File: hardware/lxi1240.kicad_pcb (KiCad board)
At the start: 2 copper layers, 105.4 x 62.2 mm, 1 part, among them J230 1240COMM

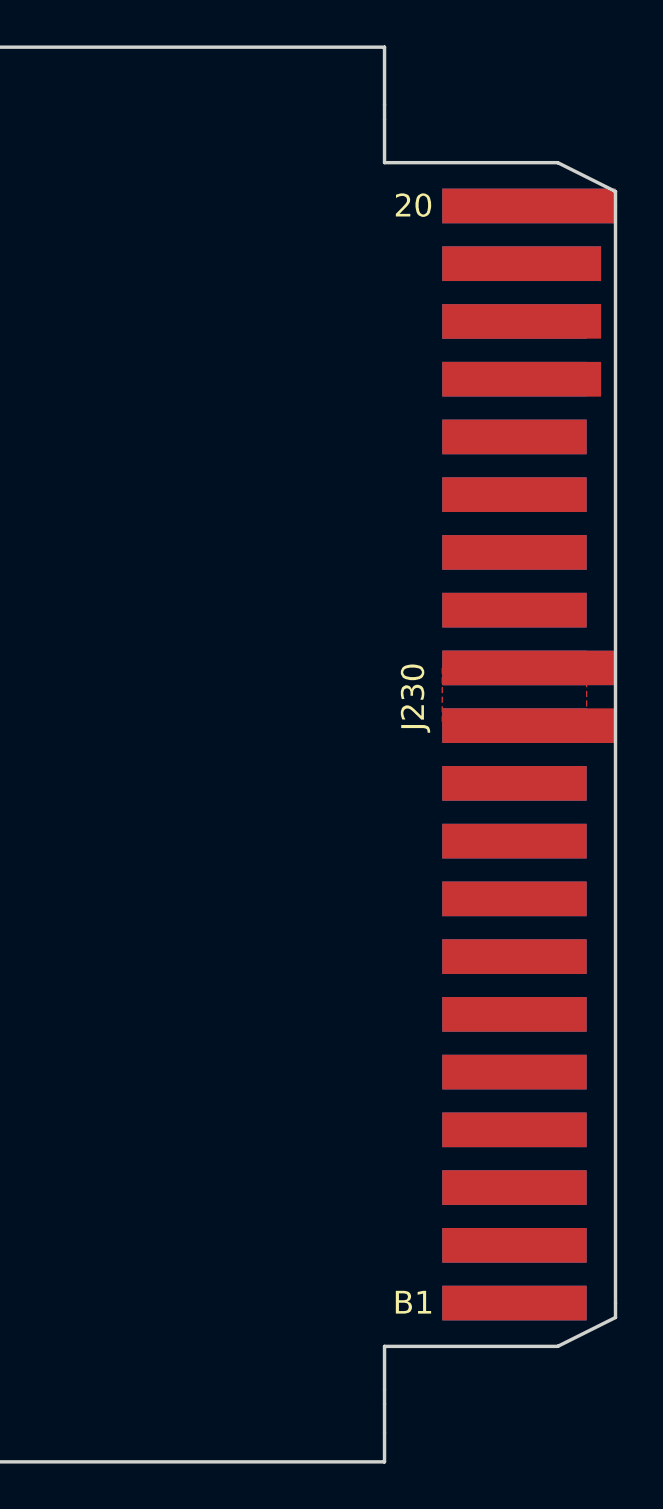
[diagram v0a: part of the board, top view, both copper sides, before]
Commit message: Add a breakout header for the board edge connector.
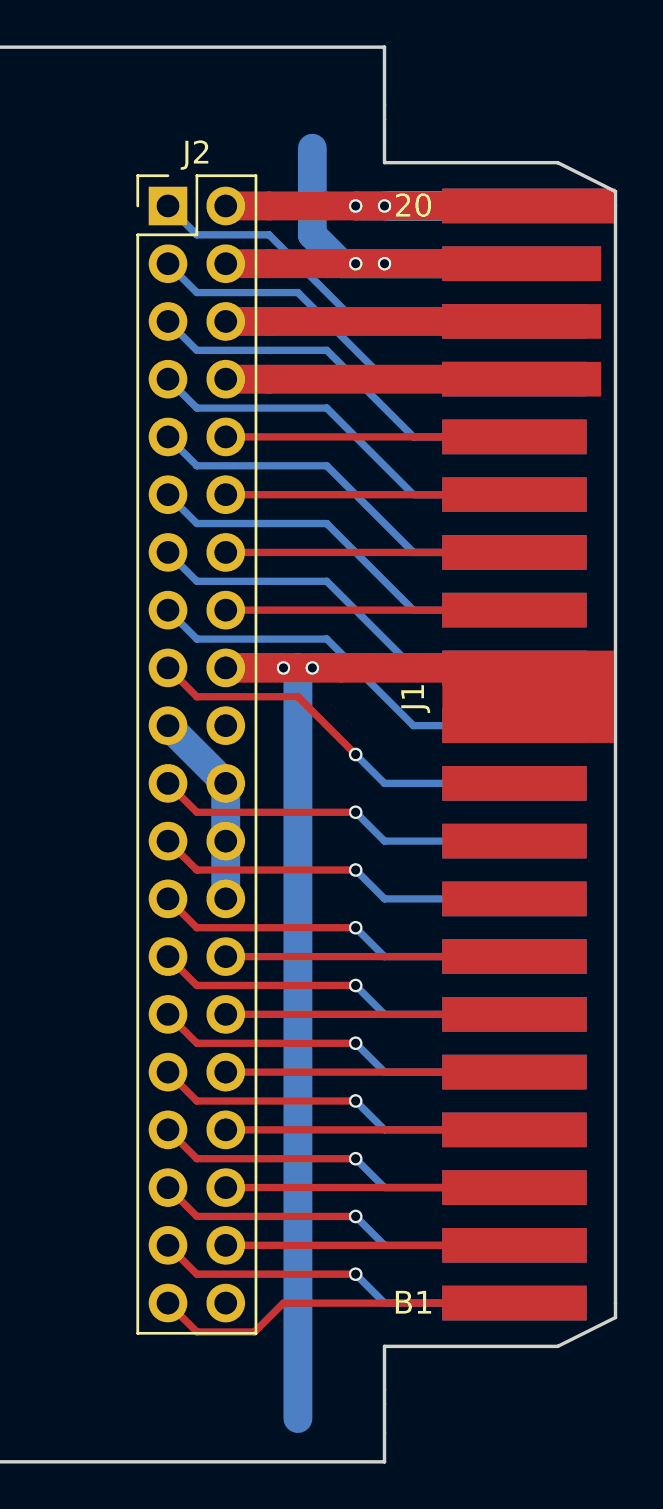
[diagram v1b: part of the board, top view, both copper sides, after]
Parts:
- added J2: 1240COMM_EXT, Pin_Headers:Pin_Header_Straight_2x20_Pitch2.54mm, F.Cu at (205.1, 64.8)
- renumbered J230 to J1
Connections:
- J1 pad A1: Net-(J230-PadA1) -> /~H-WR
- J1 pad A10: /D2 -> /H-D2
- J1 pad A11: /D0 -> /H-D0
- J1 pad A13: Net-(J230-PadA13) -> /~H-RS
- J1 pad A14: Net-(J230-PadA14) -> /H-INT
- J1 pad A15: Net-(J230-PadA15) -> /~H-RD
- J1 pad A16: /A0 -> /H-A0
- J1 pad A17: /A2 -> /H-A2
- J1 pad A18: /A4 -> /H-A4
- J1 pad A2: Net-(J230-PadA2) -> /H-RST
- J1 pad A3: /A5 -> /H-A5
- J1 pad A4: /D1 -> /H-D1
- J1 pad A5: /D3 -> /H-D3
- J1 pad A6: /D5 -> /H-D5
- J1 pad A7: /D7 -> /H-D7
- J1 pad A8: /D6 -> /H-D6
- J1 pad A9: /D4 -> /H-D4
- J1 pad B1: /A1 -> /H-A1
- J1 pad B13: /A12 -> /H-A12
- J1 pad B14: /A10 -> /H-A10
- J1 pad B15: /A8 -> /H-A8
- J1 pad B16: /A6 -> /H-A6
- J1 pad B17: Net-(J230-PadB17) -> +12VA
- J1 pad B18: Net-(J230-PadB18) -> -12VA
- J1 pad B2: /A3 -> /H-A3
- J1 pad B3: Net-(J230-PadB3) -> /~H-CS
- J1 pad B4: /A7 -> /H-A7
- J1 pad B5: /A9 -> /H-A9
- J1 pad B6: /A11 -> /H-A11
- J1 pad B7: /A13 -> /H-A13
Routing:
- net Earth_Protective: track 0.00 -> 52.1 mm, vias 0 -> 2
- net GND: track 0.00 -> 24.5 mm, vias 0 -> 2
- net +5V: track 0.00 -> 22.1 mm, vias 0 -> 2
- net /H-A0: track 0.00 -> 14.2 mm
- net Net-(J1-PadA12): track 0.00 -> 14.2 mm
- net /~H-RS: track 0.00 -> 14.2 mm
- net /~H-RD: track 0.00 -> 14.2 mm
- net /H-INT: track 0.00 -> 14.2 mm
- net /H-D2: track 0.00 -> 14.2 mm, vias 0 -> 1
- net /H-D0: track 0.00 -> 14.2 mm
- net /H-A4: track 0.00 -> 14.2 mm
- net /H-A2: track 0.00 -> 14.2 mm
- net /~H-WR: track 0.00 -> 13.1 mm, vias 0 -> 1
- net /H-D7: track 0.00 -> 13.1 mm, vias 0 -> 1
- net /H-D6: track 0.00 -> 13.1 mm, vias 0 -> 1
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- removed copper zone on F.Cu, net Earth_Protective
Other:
- net class Default: trace_width 0.25 -> 0.32258
- net class Power added: clearance 0.2, trace_width 1.27, via_dia 0.6, via_drill 0.4
- net class SGND removed
- rule trace_min: 0.2 -> 0.1524
- rule via_min_drill: 0.3 -> 0.254
- rule via_min_size: 0.4 -> 0.254
- board text added: "+12"
- board text added: "+5"
- board text added: "-12"
- board text added: "A0"
- board text added: "A1"
- board text added: "A10"
- board text added: "A11"
- board text added: "A12"
- board text added: "A13"
- board text added: "A2"
- board text added: "A3"
- board text added: "A4"
- board text added: "A5"
- board text added: "A6"
- board text added: "A7"
- board text added: "A8"
- board text added: "A9"
- board text added: "D0"
- board text added: "D1"
- board text added: "D2"
- board text added: "D3"
- board text added: "D4"
- board text added: "D5"
- board text added: "D6"
- board text added: "D7"
- board text added: "GND"
- board text added: "INT"
- board text added: "OSC"
- board text added: "PE"
- board text added: "RST"
- board text added: "USE 80-CONDUCTOR ATA RIBBON"
- board text added: "~CS"
- board text added: "~RD"
- board text added: "~RS"
- board text added: "~WR"

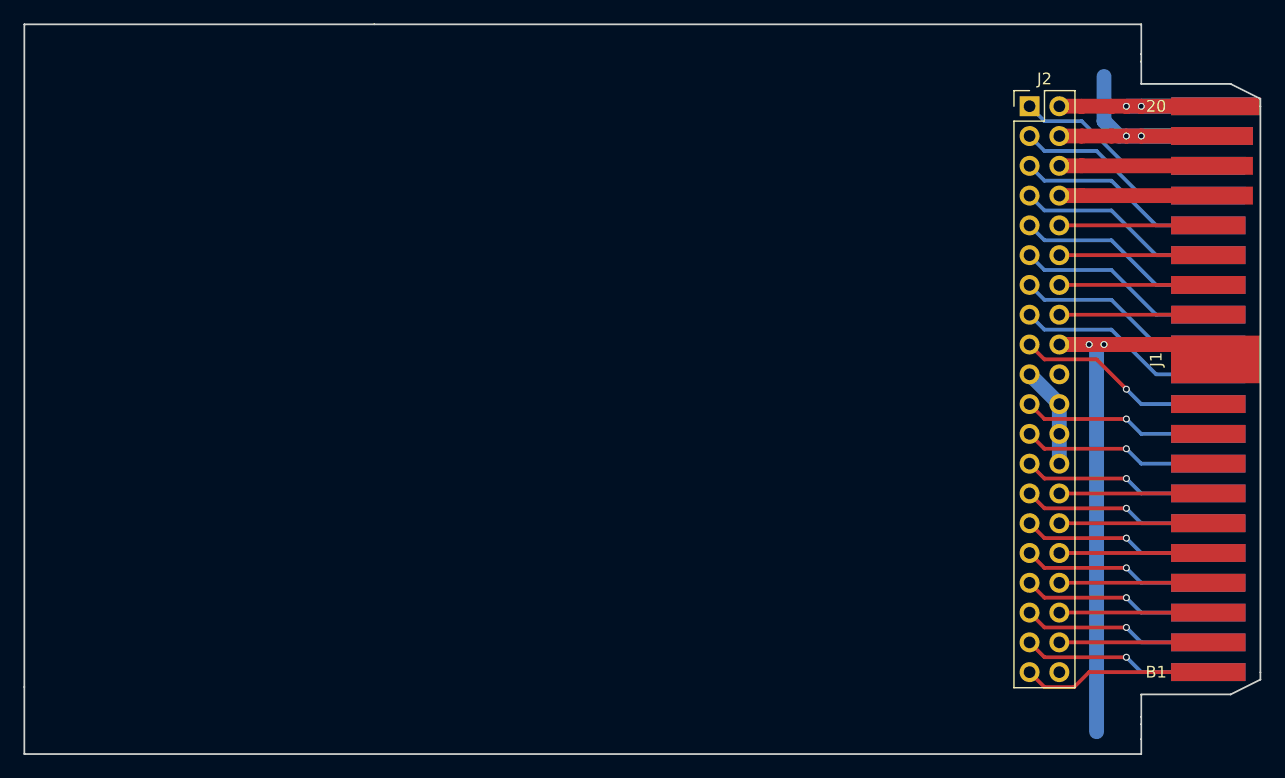
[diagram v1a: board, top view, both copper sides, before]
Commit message: Add mounting holes with protective ground.
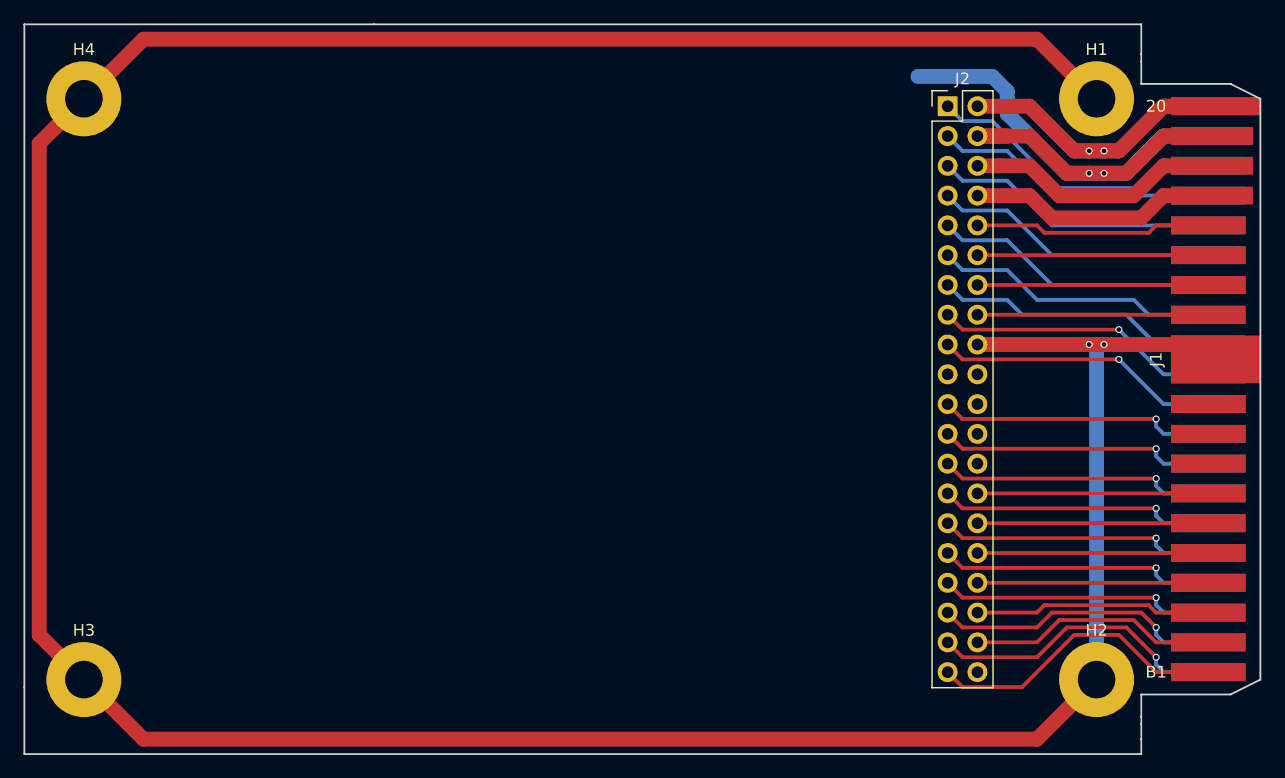
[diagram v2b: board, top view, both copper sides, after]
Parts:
- added H1: Mount, Mounting_Holes:MountingHole_3.2mm_M3_Pad, F.Cu at (210.8, 64.1)
- added H2: Mount, Mounting_Holes:MountingHole_3.2mm_M3_Pad, F.Cu at (210.8, 113.7)
- added H3: Mount, Mounting_Holes:MountingHole_3.2mm_M3_Pad, F.Cu at (124.5, 113.7)
- added H4: Mount, Mounting_Holes:MountingHole_3.2mm_M3_Pad, F.Cu at (124.5, 64.1)
- moved J2 6.98 mm to (198.1, 64.8)
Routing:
- net Earth_Protective: track 52.1 -> 280.2 mm
- net +5V: track 22.1 -> 52.7 mm
- net GND: track 24.5 -> 38.5 mm
- net /H-A1: track 13.1 -> 22.7 mm
- net /~H-WR: track 13.1 -> 22.6 mm
- net -12VA: track 9.52 -> 18.6 mm
- net /H-A3: track 9.52 -> 18.1 mm
- net +12VA: track 9.52 -> 18.1 mm
- net /H-A4: track 14.2 -> 22.7 mm
- net /H-RST: track 13.1 -> 21.5 mm
- net /~H-CS: track 9.52 -> 17.0 mm
- net /H-A6: track 9.52 -> 17.0 mm
- net /H-D7: track 13.1 -> 20.5 mm
- net /H-D4: track 13.1 -> 20.5 mm
- net /H-D3: track 13.1 -> 20.5 mm
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
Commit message: Add ground pours.
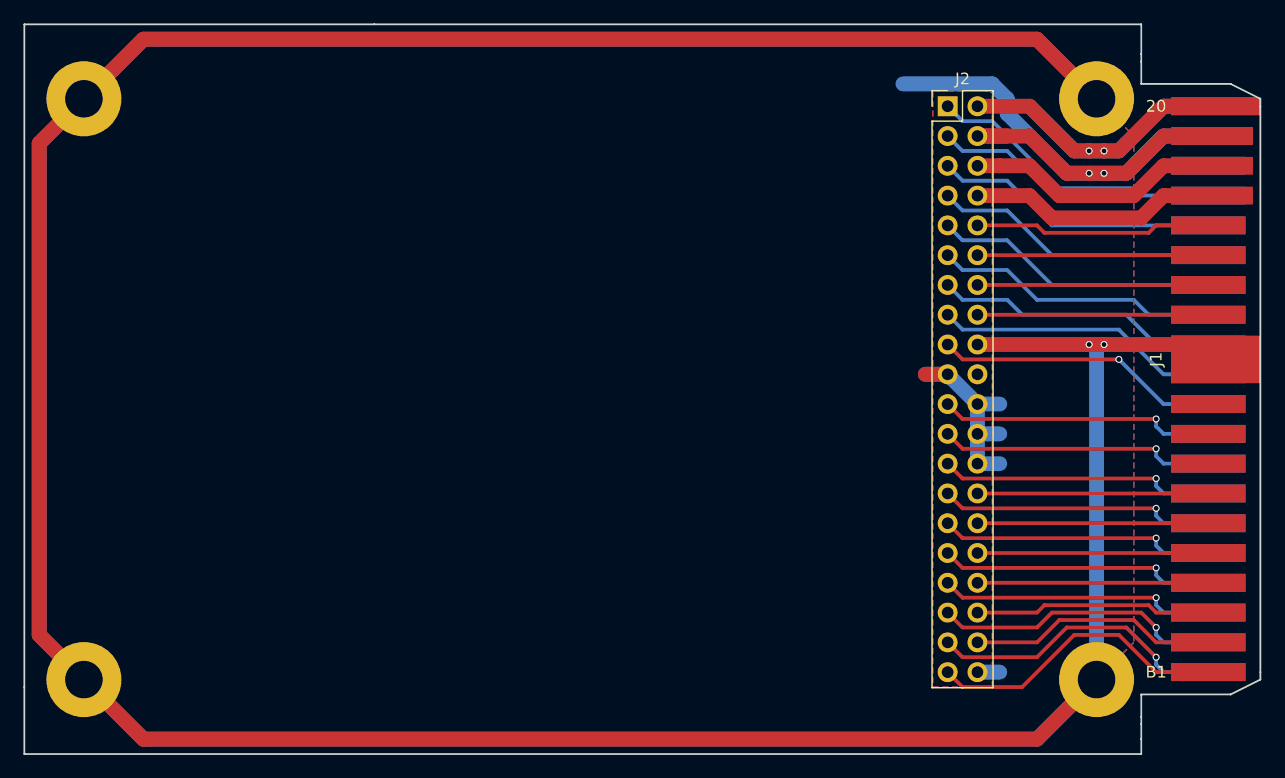
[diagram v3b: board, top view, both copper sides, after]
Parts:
- renumbered H2 to H1, H3 to H2, H4 to H3, H1 to H4
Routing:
- net Earth_Protective: track 280.2 -> 514.0 mm
- net GND: track 38.5 -> 58.6 mm
- net +5V: track 52.7 -> 53.3 mm
- net /H-D0: vias 1 -> 0
- added copper zone on B.Cu, net GND
- added copper zone on F.Cu, net GND

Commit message: Remove pad for key pin in ATA header.
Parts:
- J2: footprint Pin_Headers:Pin_Header_Straight_2x20_Pitch2.54mm -> 1240comm:ATA_HEADER
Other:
- board text added: "USE 80-CONDUCTOR ATA RIBBON DO NOT USE SLAVE CONNECTOR"
- board text removed: "USE 80-CONDUCTOR ATA RIBBON"
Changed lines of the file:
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@@
     (zones 0)
     (modules 6)
-    (nets 39)
+    (nets 38)
   )
   (page A4)
@@
     (46 B.CrtYd user)
     (47 F.CrtYd user)
-    (48 B.Fab user hide)
-    (49 F.Fab user hide)
+    (48 B.Fab user)
+    (49 F.Fab user)
   )
   (setup
@@
     (pad_to_mask_clearance 0.2)
     (aux_axis_origin 0 0)
-    (visible_elements FFFEFFFF)
+    (visible_elements FFFEEF7F)
     (pcbplotparams
       (layerselection 0x00030_80000001)
@@
   (net 36 /H-A2)
   (net 37 /H-A4)
-  (net 38 "Net-(J2-Pad20)")
   (net_class Default "This is the default net class."
     (clearance 0.2)
@@
     (add_net "Net-(J1-PadB8)")
     (add_net "Net-(J1-PadB9)")
-    (add_net "Net-(J2-Pad20)")
   )
   (net_class Power ""
@@
       (net 1 GND))
   )
-  (module Pin_Headers:Pin_Header_Straight_2x20_Pitch2.54mm (layer F.Cu)
+  (module Mounting_Holes:MountingHole_3.2mm_M3_Pad (layer F.Cu)
+    (at 210.82 64.135)
+    (descr "Mounting Hole 3.2mm, M3")
+    (tags "mounting hole 3.2mm m3")
+    (attr virtual)
+    (fp_text reference H4 (at 0 -4.445) (layer F.SilkS) hide
+      (effects (font (size 1 1) (thickness 0.15)))
+    )
+    (fp_text value Mount (at 0 4.2) (layer F.Fab)
+      (effects (font (size 1 1) (thickness 0.15)))
+    )
+    (fp_text user %R (at 0.3 0) (layer F.Fab)
+      (effects (font (size 1 1) (thickness 0.15)))
+    )
+    (fp_circle (center 0 0) (end 3.2 0) (layer Cmts.User) (width 0.15))
+    (fp_circle (center 0 0) (end 3.45 0) (layer F.CrtYd) (width 0.05))
+    (pad 1 thru_hole circle (at 0 0) (size 6.4 6.4) (drill 3.2) (layers *.Cu *.Mask)
+      (net 3 Earth_Protective))
+  )
+  (module Mounting_Holes:MountingHole_3.2mm_M3_Pad (layer F.Cu)
+    (at 210.82 113.665)
+    (descr "Mounting Hole 3.2mm, M3")
+    (tags "mounting hole 3.2mm m3")
+    (attr virtual)
+    (fp_text reference H1 (at 0 4.445) (layer F.SilkS) hide
+      (effects (font (size 1 1) (thickness 0.15)))
+    )
+    (fp_text value Mount (at 0 4.2) (layer F.Fab)
+      (effects (font (size 1 1) (thickness 0.15)))
+    )
+    (fp_text user %R (at 0.3 0) (layer F.Fab)
+      (effects (font (size 1 1) (thickness 0.15)))
+    )
+    (fp_circle (center 0 0) (end 3.2 0) (layer Cmts.User) (width 0.15))
+    (fp_circle (center 0 0) (end 3.45 0) (layer F.CrtYd) (width 0.05))
+    (pad 1 thru_hole circle (at 0 0) (size 6.4 6.4) (drill 3.2) (layers *.Cu *.Mask)
+      (net 3 Earth_Protective))
+  )
+  (module Mounting_Holes:MountingHole_3.2mm_M3_Pad (layer F.Cu)
+    (at 124.46 113.665)
+    (descr "Mounting Hole 3.2mm, M3")
+    (tags "mounting hole 3.2mm m3")
+    (attr virtual)
+    (fp_text reference H2 (at 0 4.445) (layer F.SilkS) hide
+      (effects (font (size 1 1) (thickness 0.15)))
+    )
+    (fp_text value Mount (at 0 4.2) (layer F.Fab)
+      (effects (font (size 1 1) (thickness 0.15)))
+    )
+    (fp_text user %R (at 0.3 0) (layer F.Fab)
+      (effects (font (size 1 1) (thickness 0.15)))
+    )
+    (fp_circle (center 0 0) (end 3.2 0) (layer Cmts.User) (width 0.15))
+    (fp_circle (center 0 0) (end 3.45 0) (layer F.CrtYd) (width 0.05))
+    (pad 1 thru_hole circle (at 0 0) (size 6.4 6.4) (drill 3.2) (layers *.Cu *.Mask)
+      (net 3 Earth_Protective))
+  )
+  (module Mounting_Holes:MountingHole_3.2mm_M3_Pad (layer F.Cu)
+    (at 124.46 64.135)
+    (descr "Mounting Hole 3.2mm, M3")
+    (tags "mounting hole 3.2mm m3")
+    (attr virtual)
+    (fp_text reference H3 (at 0 -4.445) (layer F.SilkS) hide
+      (effects (font (size 1 1) (thickness 0.15)))
+    )
+    (fp_text value Mount (at 0 4.2) (layer F.Fab)
+      (effects (font (size 1 1) (thickness 0.15)))
+    )
+    (fp_text user %R (at 0.3 0) (layer F.Fab)
+      (effects (font (size 1 1) (thickness 0.15)))
+    )
+    (fp_circle (center 0 0) (end 3.2 0) (layer Cmts.User) (width 0.15))
+    (fp_circle (center 0 0) (end 3.45 0) (layer F.CrtYd) (width 0.05))
+    (pad 1 thru_hole circle (at 0 0) (size 6.4 6.4) (drill 3.2) (layers *.Cu *.Mask)
+      (net 3 Earth_Protective))
+  )
+  (module 1240comm:ATA_HEADER (layer F.Cu)
     (at 198.12 64.77)
     (descr "Through hole straight pin header, 2x20, 2.54mm pitch, double rows")
@@
     (pad 19 thru_hole oval (at 0 22.86) (size 1.7 1.7) (drill 1) (layers *.Cu *.Mask)
       (net 1 GND))
-    (pad 20 thru_hole oval (at 2.54 22.86) (size 1.7 1.7) (drill 1) (layers *.Cu *.Mask)
-      (net 38 "Net-(J2-Pad20)"))
     (pad 21 thru_hole oval (at 0 25.4) (size 1.7 1.7) (drill 1) (layers *.Cu *.Mask)
       (net 28 /H-D4))
@@
     )
   )
-  (module Mounting_Holes:MountingHole_3.2mm_M3_Pad (layer F.Cu)
-    (at 210.82 64.135)
-    (descr "Mounting Hole 3.2mm, M3")
-    (tags "mounting hole 3.2mm m3")
-    (attr virtual)
-    (fp_text reference H4 (at 0 -4.445) (layer F.SilkS) hide
-      (effects (font (size 1 1) (thickness 0.15)))
-    )
-    (fp_text value Mount (at 0 4.2) (layer F.Fab)
-      (effects (font (size 1 1) (thickness 0.15)))
-    )
-    (fp_text user %R (at 0.3 0) (layer F.Fab)
-      (effects (font (size 1 1) (thickness 0.15)))
-    )
-    (fp_circle (center 0 0) (end 3.2 0) (layer Cmts.User) (width 0.15))
-    (fp_circle (center 0 0) (end 3.45 0) (layer F.CrtYd) (width 0.05))
-    (pad 1 thru_hole circle (at 0 0) (size 6.4 6.4) (drill 3.2) (layers *.Cu *.Mask)
-      (net 3 Earth_Protective))
-  )
-  (module Mounting_Holes:MountingHole_3.2mm_M3_Pad (layer F.Cu)
-    (at 210.82 113.665)
-    (descr "Mounting Hole 3.2mm, M3")
-    (tags "mounting hole 3.2mm m3")
-    (attr virtual)
-    (fp_text reference H1 (at 0 4.445) (layer F.SilkS) hide
-      (effects (font (size 1 1) (thickness 0.15)))
-    )
-    (fp_text value Mount (at 0 4.2) (layer F.Fab)
-      (effects (font (size 1 1) (thickness 0.15)))
-    )
-    (fp_text user %R (at 0.3 0) (layer F.Fab)
-      (effects (font (size 1 1) (thickness 0.15)))
-    )
-    (fp_circle (center 0 0) (end 3.2 0) (layer Cmts.User) (width 0.15))
-    (fp_circle (center 0 0) (end 3.45 0) (layer F.CrtYd) (width 0.05))
-    (pad 1 thru_hole circle (at 0 0) (size 6.4 6.4) (drill 3.2) (layers *.Cu *.Mask)
-      (net 3 Earth_Protective))
-  )
-  (module Mounting_Holes:MountingHole_3.2mm_M3_Pad (layer F.Cu)
-    (at 124.46 113.665)
-    (descr "Mounting Hole 3.2mm, M3")
-    (tags "mounting hole 3.2mm m3")
-    (attr virtual)
-    (fp_text reference H2 (at 0 4.445) (layer F.SilkS) hide
-      (effects (font (size 1 1) (thickness 0.15)))
-    )
-    (fp_text value Mount (at 0 4.2) (layer F.Fab)
-      (effects (font (size 1 1) (thickness 0.15)))
-    )
-    (fp_text user %R (at 0.3 0) (layer F.Fab)
-      (effects (font (size 1 1) (thickness 0.15)))
-    )
-    (fp_circle (center 0 0) (end 3.2 0) (layer Cmts.User) (width 0.15))
-    (fp_circle (center 0 0) (end 3.45 0) (layer F.CrtYd) (width 0.05))
-    (pad 1 thru_hole circle (at 0 0) (size 6.4 6.4) (drill 3.2) (layers *.Cu *.Mask)
-      (net 3 Earth_Protective))
-  )
-  (module Mounting_Holes:MountingHole_3.2mm_M3_Pad (layer F.Cu)
-    (at 124.46 64.135)
-    (descr "Mounting Hole 3.2mm, M3")
-    (tags "mounting hole 3.2mm m3")
-    (attr virtual)
-    (fp_text reference H3 (at 0 -4.445) (layer F.SilkS) hide
-      (effects (font (size 1 1) (thickness 0.15)))
-    )
-    (fp_text value Mount (at 0 4.2) (layer F.Fab)
-      (effects (font (size 1 1) (thickness 0.15)))
-    )
-    (fp_text user %R (at 0.3 0) (layer F.Fab)
-      (effects (font (size 1 1) (thickness 0.15)))
-    )
-    (fp_circle (center 0 0) (end 3.2 0) (layer Cmts.User) (width 0.15))
-    (fp_circle (center 0 0) (end 3.45 0) (layer F.CrtYd) (width 0.05))
-    (pad 1 thru_hole circle (at 0 0) (size 6.4 6.4) (drill 3.2) (layers *.Cu *.Mask)
-      (net 3 Earth_Protective))
-  )
-  (gr_text "USE 80-CONDUCTOR ATA RIBBON" (at 208.915 87.63 270) (layer B.SilkS)
+  (gr_text "USE 80-CONDUCTOR ATA RIBBON\nDO NOT USE SLAVE CONNECTOR" (at 210.185 88.9 270) (layer B.SilkS)
     (effects (font (size 1.5 1.5) (thickness 0.3)) (justify mirror))
   )
